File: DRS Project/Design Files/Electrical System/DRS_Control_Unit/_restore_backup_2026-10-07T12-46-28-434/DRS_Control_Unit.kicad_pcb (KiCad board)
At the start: 2 copper layers, 100 x 100 mm, 37 parts, among them IC1 AP63301QWU-7, J1 Deutsch DT, J2 Screw, J3 Servo, J5 DE9_Socket, SW1 DSIC01THGET, U1 AMS1117, U7 Teensy4.0-NU-Teams, U8 TJA1051T-3

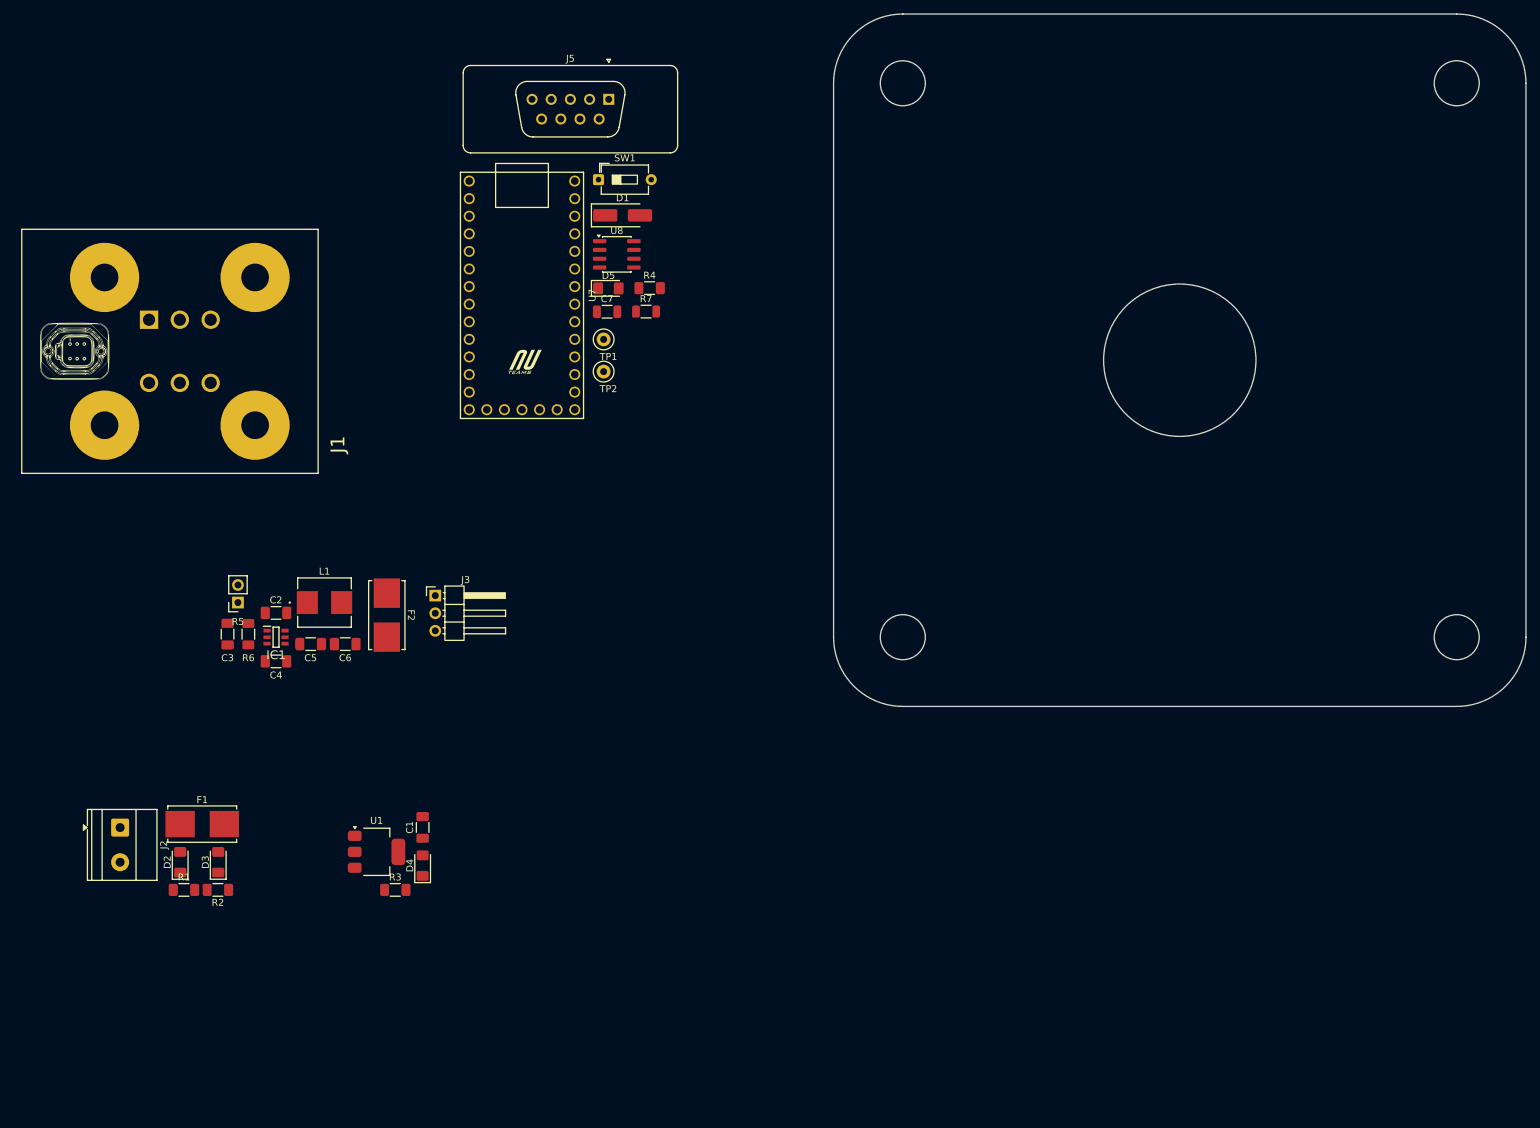
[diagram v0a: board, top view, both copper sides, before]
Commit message: DDR started and circuit edited to fit DDR
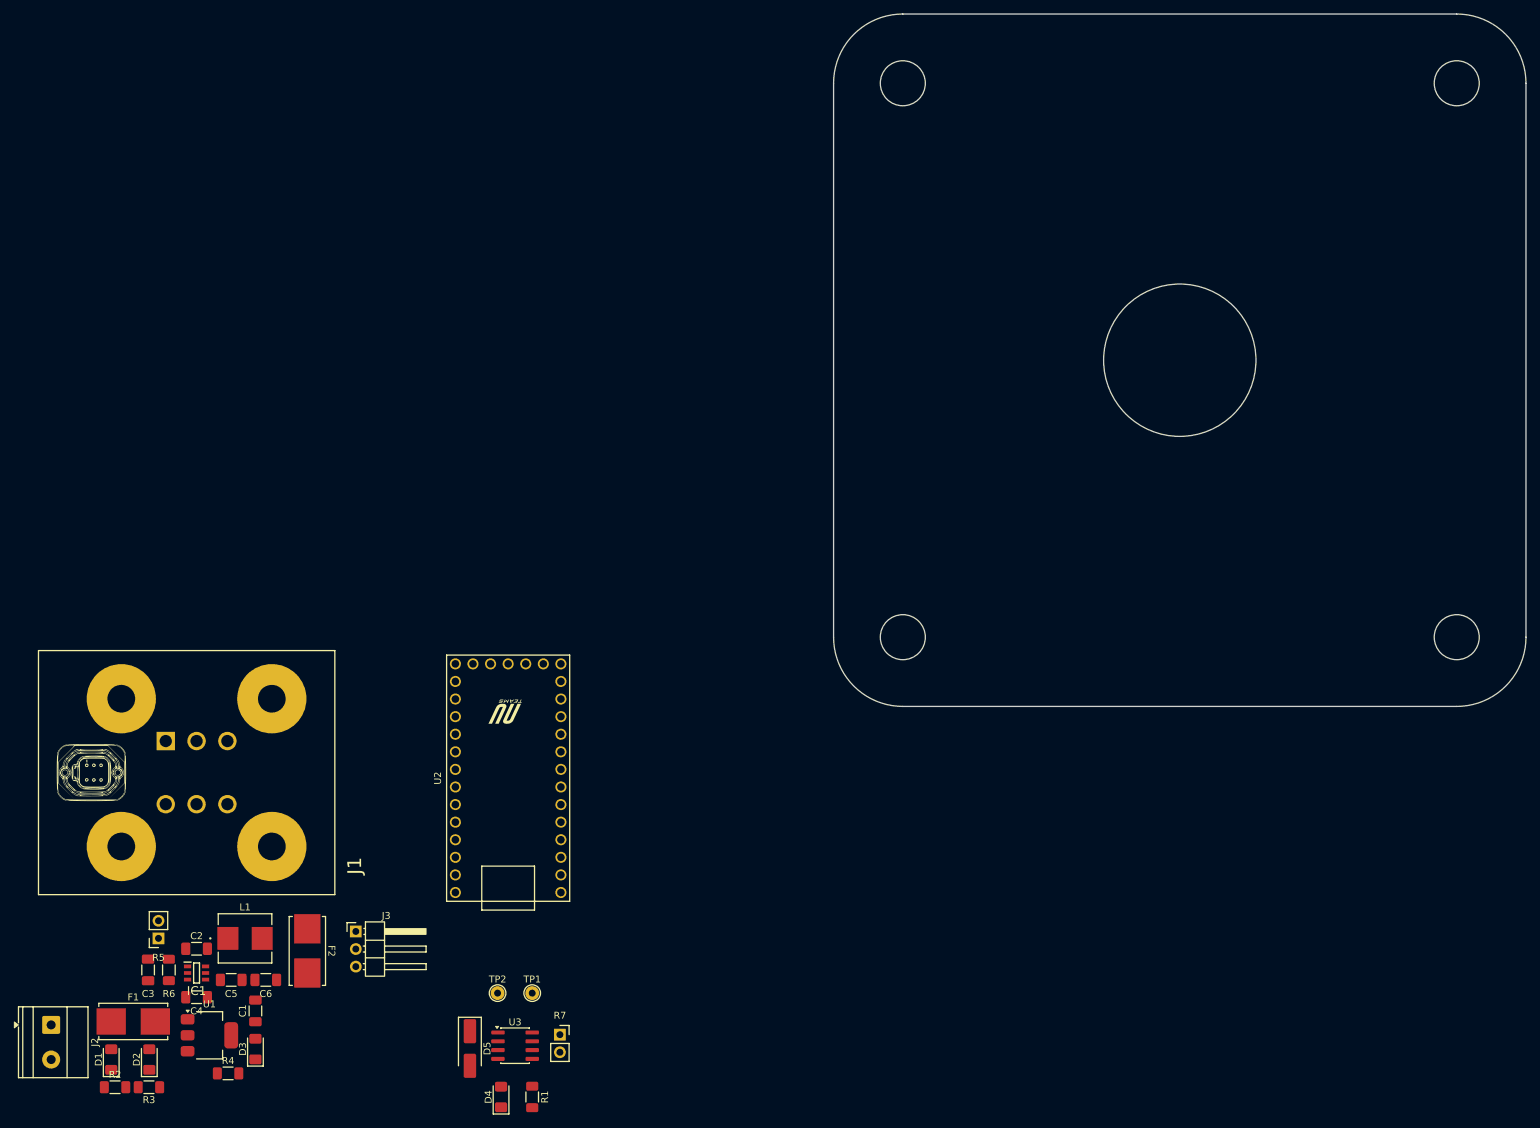
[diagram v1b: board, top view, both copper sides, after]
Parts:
- removed C7: 0.1uF, Capacitor_SMD:C_1206_3216Metric
- removed the D1 at (106.5, 63.1)
- removed J5: DE9_Socket, Connector_Dsub:DSUB-9_Socket_Vertical_P2.77x2.84mm
- removed the R4 at (110.4, 73.6)
- removed SW1: DSIC01THGET, Button_Switch_THT:SW_DIP_SPSTx01_Slide_6.7x4.1mm_W7.62mm_P2.54mm_LowProfile
- removed U7: Teensy4.0-NU-Teams, NU-Teams-Footprints:Teensy4.0-NU-Teams
- removed U8: TJA1051T-3, Package_SO:SOIC-8_3.9x4.9mm_P1.27mm
- added D4: +5V PROT, LED_SMD:LED_1206_3216Metric_Pad1.42x1.75mm_HandSolder, F.Cu at (89.0, 190.4)
- added R1: 330R, Resistor_SMD:R_1206_3216Metric_Pad1.30x1.75mm_HandSolder, F.Cu at (93.5, 190.4)
- added U2: Teensy4.0-NU-Teams, NU-Teams-Footprints:Teensy4.0-NU-Teams, F.Cu at (97.6, 160.9)
- added U3: TJA1051T-3, Package_SO:SOIC-8_3.9x4.9mm_P1.27mm, F.Cu at (91.0, 183.0)
- D5: value +5V PROT -> SS34; footprint LED_SMD:LED_1206_3216Metric_Pad1.42x1.75mm_HandSolder -> Diode_SMD:D_SMA_Handsoldering
- R7: value 120Ω -> R; footprint Resistor_SMD:R_1206_3216Metric -> Connector_PinSocket_2.54mm:PinSocket_1x02_P2.54mm_Vertical
- TP1: value CAN_H1 -> CANH; footprint TestPoint:TestPoint_Loop_D1.80mm_Drill1.0mm_Beaded -> TestPoint:TestPoint_THTPad_D2.0mm_Drill1.0mm
- TP2: value CAN_L1 -> CANL; footprint TestPoint:TestPoint_Loop_D1.80mm_Drill1.0mm_Beaded -> TestPoint:TestPoint_THTPad_D2.0mm_Drill1.0mm
- moved D5 111.6 mm to (84.5, 183.4), turned to -90 degrees
- moved R7 105.2 mm to (97.5, 181.4)
- moved TP1 95.0 mm to (93.5, 175.4)
- moved TP2 91.1 mm to (88.5, 175.4)
- moved J1 60.9 mm to (43.0, 143.6)
- moved C2 49.8 mm to (45.0, 169.0)
- moved C3 49.8 mm to (38.0, 172.1)
- moved C4 49.8 mm to (45.0, 176.0)
- moved C5 49.8 mm to (50.0, 173.5)
- moved C6 49.8 mm to (55.0, 173.5)
- moved F2 49.8 mm to (61.0, 169.3)
- moved IC1 49.8 mm to (45.0, 172.5)
- moved J3 49.8 mm to (68.0, 166.5)
- moved L1 49.8 mm to (52.0, 167.5)
- moved R5 49.8 mm to (39.5, 167.5)
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- renumbered D2 to D1, D3 to D2, D4 to D3, R1 to R2, R2 to R3, R3 to R4
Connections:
- net Net-(IC1-FB) renamed /FB
- C1 pad 1: Net-(D1-A) -> +5V
- D3 pad 2: Net-(D1-A) -> +5V
- R7 pad 2: Net-(R7-Pad2) -> /CAN LOW
- U1 pad 2: Net-(D1-A) -> +5V
